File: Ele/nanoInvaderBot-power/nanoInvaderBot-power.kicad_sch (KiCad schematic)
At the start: 10 parts, among them J1 S6B-ZR-SM4A-TF(LF)(SN), J2 S6B-ZR-SM4A-TF(LF)(SN), J3 1746142-1, U3 MP2672AGD-0000-Z

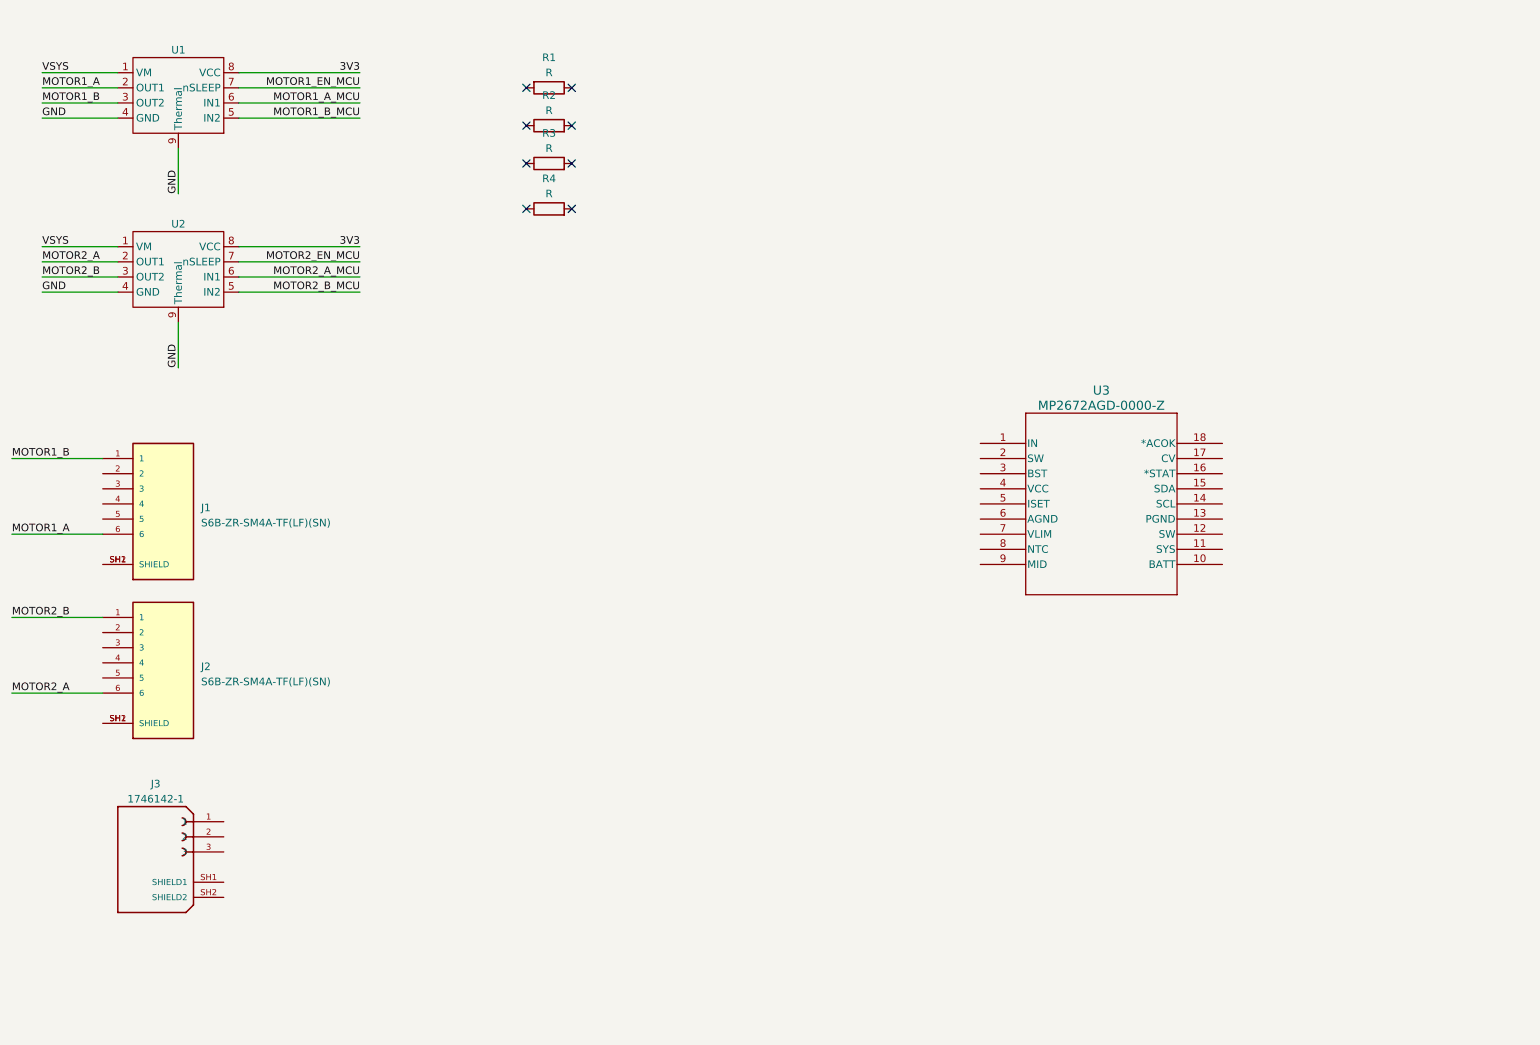
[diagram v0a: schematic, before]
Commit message: Placed components in power board
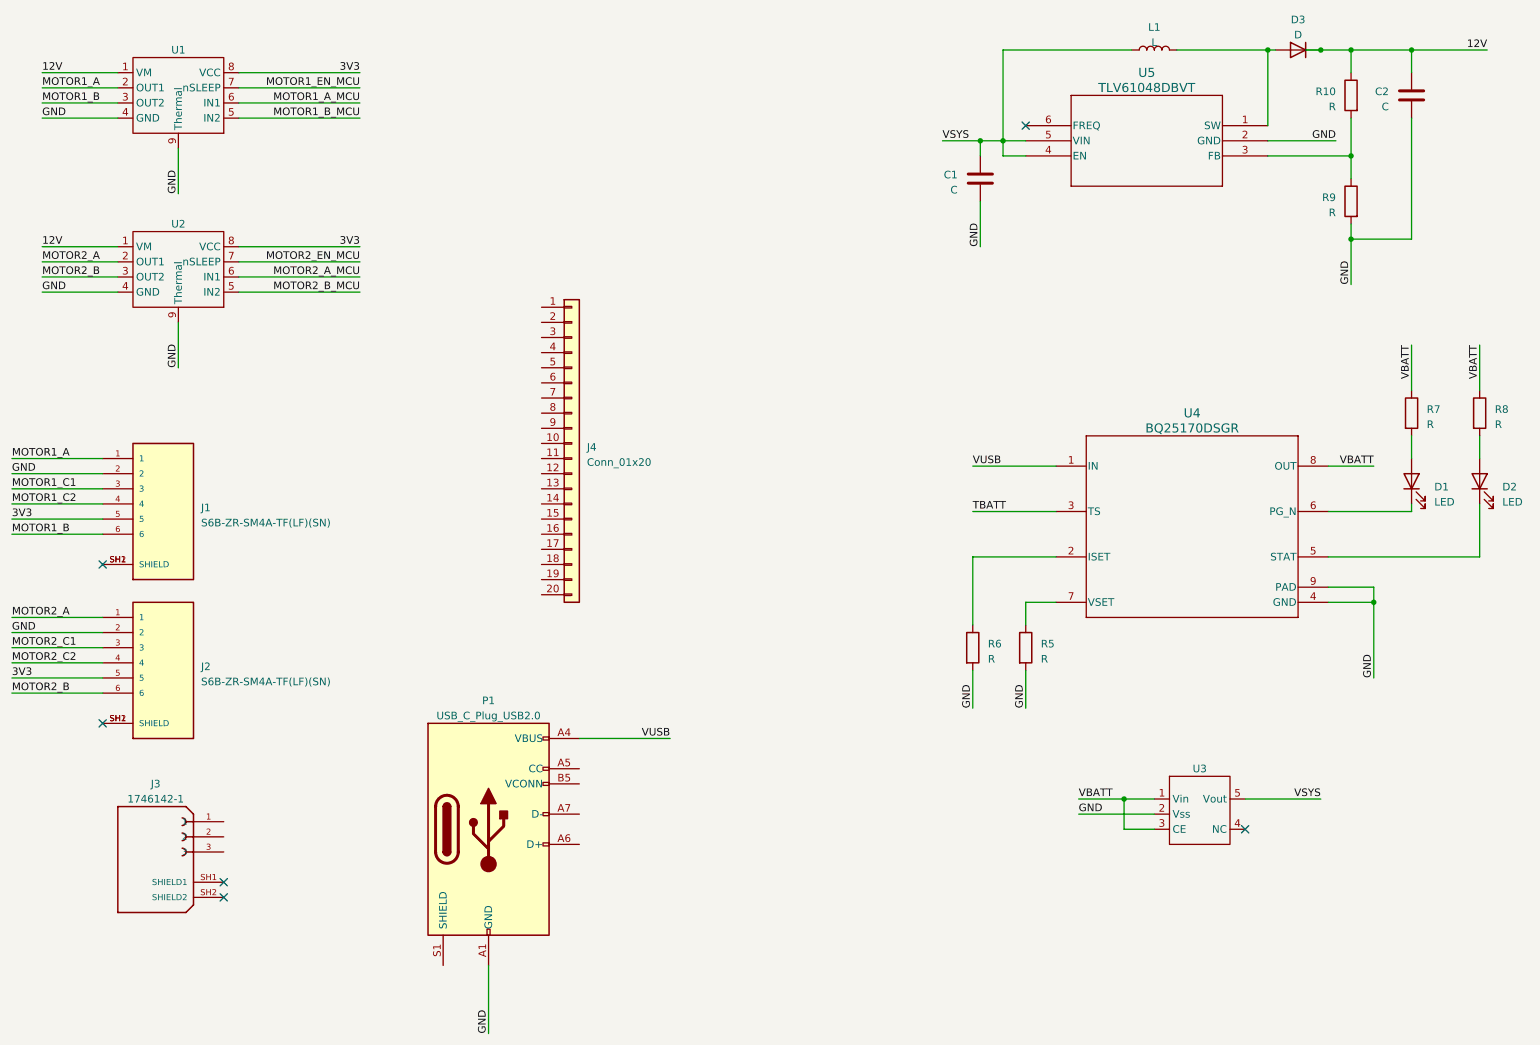
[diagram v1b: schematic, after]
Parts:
- removed R1, R2, R3, R4: R, Resistor_SMD:R_1206_3216Metric, symbol Device:R
- removed U3: MP2672AGD-0000-Z, Components:QFN-18_MP2672A_MNP, symbol MP2672:MP2672AGD-0000-Z
- added C1, C2: C, symbol Device:C
- added D1, D2: LED, LED_SMD:LED_0603_1608Metric, symbol Device:LED
- added D3: D, symbol Device:D
- added J4: Conn_01x20, footprints:TE_2-1734839-0, symbol Connector_Generic:Conn_01x20
- added L1: L, symbol Device:L
- added P1: USB_C_Plug_USB2.0, Connector_USB:USB_C_Receptacle_GCT_USB4135-GF-A_6P_TopMnt_Horizontal, symbol Connector:USB_C_Plug_USB2.0
- added R10, R9: R, symbol Device:R
- added R5, R6, R7, R8: R, Resistor_SMD:R_0603_1608Metric, symbol Device:R
- added U3: ~, Package_TO_SOT_SMD:SOT-23-5, symbol XC8111:XC8111-MR-G
- added U4: BQ25170DSGR, footprints:BQ25170DSGR_NV, symbol BQ25170DSGR:BQ25170DSGR
- added U5: TLV61048DBVT, SOT23-6_DBV_TEX, symbol TLV61048DBVT:TLV61048DBVT
- J1, J2: footprint Components:JST_S6B-ZR-SM4A-TF(LF)(SN) -> footprints:JST_S6B-ZR-SM4A-TF(LF)(SN)
- J3: footprint Components:TE_1746142-1 -> footprints:TE_1746142-1
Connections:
- net 3V3: now also J1.5, J2.5
- net GND: now also J1.2, J2.2, C1.2, C2.2, P1.A1 (GND), P1.A12 (GND), P1.B1 (GND), P1.B12 (GND), R5.2, R6.2, R9.2, U3.2 (Vss), U4.4 (GND), U4.9 (PAD), U5.2 (GND)
- net MOTOR1_A: now also J1.1; no longer J1.6
- net MOTOR1_B: now also J1.6; no longer J1.1
- net MOTOR2_A: now also J2.1; no longer J2.6
- net MOTOR2_B: now also J2.6; no longer J2.1
- net VSYS: now also C1.1, L1.2, U3.5 (Vout), U5.4 (EN), U5.5 (VIN); no longer U1.1 (VM), U2.1 (VM)
- net MOTOR2_C1: now reaches J2.3
- net MOTOR2_C2: now reaches J2.4
- net MOTOR1_C1: now reaches J1.3
- net MOTOR1_C2: now reaches J1.4
- new net: R6.1, U4.2 (ISET)
- new net: D2.1 (K), U4.5 (STAT)
- new net: D1.1 (K), U4.6 (PG_N)
- new net: R5.1, U4.7 (VSET)
- new net: R10.2, R9.1, U5.3 (FB)
- new net: D2.2 (A), R8.2
- new net: D1.2 (A), R7.2
- new net: D3.2 (A), L1.1, U5.1 (SW)
- new net 12V: C2.1, D3.1 (K), R10.1, U1.1 (VM), U2.1 (VM)
- new net TBATT: U4.3 (TS)
- new net VBATT: R7.1, R8.1, U3.1 (Vin), U3.3 (CE), U4.8 (OUT)
- new net VUSB: P1.A4 (VBUS), P1.A9 (VBUS), P1.B4 (VBUS), P1.B9 (VBUS), U4.1 (IN)
- no-connect marks 8 -> 6

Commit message: Intermediate state -power layer almost done
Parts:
- removed P1: USB_C_Plug_USB2.0, Connector_USB:USB_C_Receptacle_GCT_USB4135-GF-A_6P_TopMnt_Horizontal, symbol Connector:USB_C_Plug_USB2.0
- added C10, C4, C6, C7, C8, C9: C, Capacitor_SMD:C_0603_1608Metric, symbol Device:C
- added C3, C5: C, Capacitor_SMD:C_1210_3225Metric, symbol Device:C
- added R1: R, Resistor_SMD:R_0402_1005Metric, symbol Device:R
- added SW1: SW_SPDT, Button_Switch_SMD:SW_SPDT_PCM12, symbol Switch:SW_SPDT
- C1: footprint (none) -> Capacitor_SMD:C_1210_3225Metric; MPN (none) -> GCM32ER71E106KA57L
- C2: footprint (none) -> Capacitor_SMD:C_1210_3225Metric
- D1, D2: footprint LED_SMD:LED_0603_1608Metric -> Resistor_SMD:R_0402_1005Metric
- D3: footprint (none) -> footprints:SDO_B120AF_DIO
- L1: footprint (none) -> footprints:IND_SWPA5040S_SNL
- R10, R9: footprint (none) -> Resistor_SMD:R_0402_1005Metric
- R5, R6, R7, R8: footprint Resistor_SMD:R_0603_1608Metric -> Resistor_SMD:R_0402_1005Metric
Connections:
- net MOTOR1_C1 is gone; now on net MOTOR1_ENC1: J1.3
- net MOTOR1_C2 is gone; now on net MOTOR1_ENC2: J1.4
- net MOTOR2_C1 is gone; now on net MOTOR2_ENC1: J2.3
- net MOTOR2_C2 is gone; now on net MOTOR2_ENC2: J2.4
- net 12V: now also C3.1, C5.1
- net 3V3: now also J4.11 (Pin_11), C4.1, C6.1
- net GND: now also J1.SH1 (SHIELD), J1.SH2 (SHIELD), J2.SH1 (SHIELD), J2.SH2 (SHIELD), J4.17 (Pin_17), J4.18 (Pin_18), J4.3 (Pin_3), J4.4 (Pin_4), C10.2, C3.2, C4.2, C5.2, C6.2, C7.2, C8.2, C9.2, R1.2, SW1.3 (C)
- net MOTOR1_A_MCU: now also J4.6 (Pin_6)
- net MOTOR1_B_MCU: now also J4.5 (Pin_5)
- net MOTOR1_EN_MCU: now also J4.7 (Pin_7)
- net MOTOR2_A_MCU: now also J4.15 (Pin_15)
- net MOTOR2_B_MCU: now also J4.14 (Pin_14)
- net MOTOR2_EN_MCU: now also J4.16 (Pin_16)
- net VBATT: now also C8.1, C9.1, SW1.1 (A); no longer U3.3 (CE)
- net VSYS: now also J4.1 (Pin_1), J4.2 (Pin_2), C10.1
- net VUSB: now also J4.19 (Pin_19), J4.20 (Pin_20), C7.1
- net SYS_EN: now reaches J4.10 (Pin_10)
- net SYS_EN: now also U3.3 (CE), R1.1, SW1.2 (B)
- net MOTOR2_ENC1: now reaches J4.12 (Pin_12)
- net MOTOR2_ENC2: now reaches J4.13 (Pin_13)
- net MOTOR1_ENC1: now reaches J4.8 (Pin_8)
- net MOTOR1_ENC2: now reaches J4.9 (Pin_9)
- no-connect marks 6 -> 4
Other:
- moved on the sheet: D1, D3, J4, R7, U3

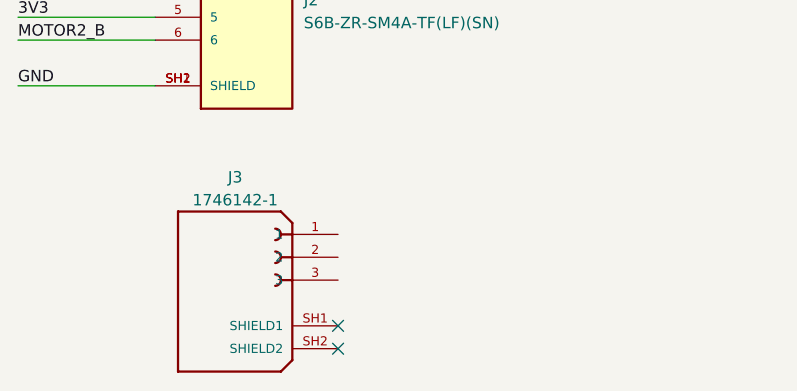
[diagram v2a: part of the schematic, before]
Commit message: Power side done, logic side cleanup
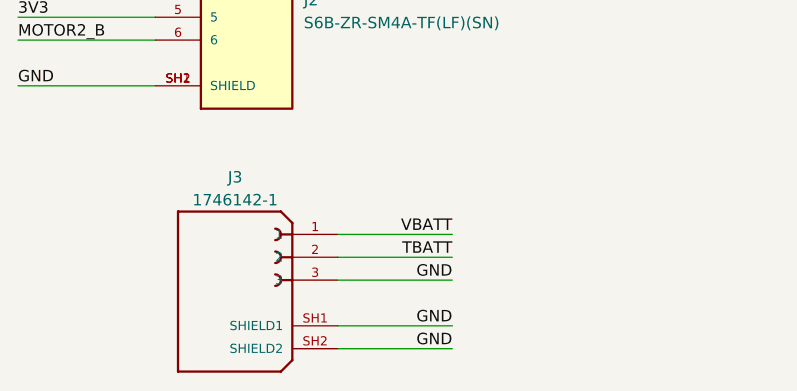
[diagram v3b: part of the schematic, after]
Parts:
- D1, D2: footprint Resistor_SMD:R_0402_1005Metric -> LED_SMD:LED_0402_1005Metric
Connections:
- net GND: now also J3.3, J3.SH1 (SHIELD1), J3.SH2 (SHIELD2)
- net TBATT: now also J3.2
- net VBATT: now also J3.1
- no-connect marks 4 -> 2
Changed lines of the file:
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@@
   (no_connect (at 229.87 146.05))
   (no_connect (at 191.77 35.56))
-  (no_connect (at 57.15 162.56))
-  (no_connect (at 57.15 165.1))
   (wire (pts (xy 191.77 115.57) (xy 196.85 115.57))
     (stroke (width 0) (type default))
@@
     (stroke (width 0) (type default))
   )
+  (wire (pts (xy 57.15 152.4) (xy 69.85 152.4))
+    (stroke (width 0) (type default))
+  )
   (wire (pts (xy 246.38 151.13) (xy 246.38 157.48))
     (stroke (width 0) (type default))
@@
     (stroke (width 0) (type default))
   )
+  (wire (pts (xy 57.15 162.56) (xy 69.85 162.56))
+    (stroke (width 0) (type default))
+  )
   (wire (pts (xy 246.38 54.61) (xy 246.38 62.23))
     (stroke (width 0) (type default))
@@
     (stroke (width 0) (type default))
   )
+  (wire (pts (xy 57.15 165.1) (xy 69.85 165.1))
+    (stroke (width 0) (type default))
+  )
   (wire (pts (xy 59.69 26.67) (xy 80.01 26.67))
     (stroke (width 0) (type default))
@@
     (stroke (width 0) (type default))
   )
+  (wire (pts (xy 57.15 157.48) (xy 69.85 157.48))
+    (stroke (width 0) (type default))
+  )
   (wire (pts (xy 246.38 40.64) (xy 246.38 34.29))
     (stroke (width 0) (type default))
@@
     (stroke (width 0) (type default))
   )
+  (wire (pts (xy 57.15 154.94) (xy 69.85 154.94))
+    (stroke (width 0) (type default))
+  )
   (wire (pts (xy 59.69 34.29) (xy 80.01 34.29))
     (stroke (width 0) (type default))
@@
     (effects (font (size 1.27 1.27)) (justify left bottom))
   )
+  (label "TBATT" (at 69.85 154.94 180) (fields_autoplaced)
+    (effects (font (size 1.27 1.27)) (justify right bottom))
+  )
   (label "GND" (at 93.98 41.91 90) (fields_autoplaced)
     (effects (font (size 1.27 1.27)) (justify left bottom))
@@
     (effects (font (size 1.27 1.27)) (justify left bottom))
   )
+  (label "GND" (at 69.85 165.1 180) (fields_autoplaced)
+    (effects (font (size 1.27 1.27)) (justify right bottom))
+  )
+  (label "VBATT" (at 69.85 152.4 180) (fields_autoplaced)
+    (effects (font (size 1.27 1.27)) (justify right bottom))
+  )
   (label "MOTOR1_B_MCU" (at 80.01 34.29 180) (fields_autoplaced)
     (effects (font (size 1.27 1.27)) (justify right bottom))
@@
     (effects (font (size 1.27 1.27)) (justify left bottom))
   )
+  (label "GND" (at 69.85 162.56 180) (fields_autoplaced)
+    (effects (font (size 1.27 1.27)) (justify right bottom))
+  )
   (label "GND" (at 243.84 38.1 180) (fields_autoplaced)
+    (effects (font (size 1.27 1.27)) (justify right bottom))
+  )
+  (label "GND" (at 69.85 157.48 180) (fields_autoplaced)
     (effects (font (size 1.27 1.27)) (justify right bottom))
   )
@@
       (effects (font (size 1.27 1.27)) (justify right))
     )
-    (property "Footprint" "Resistor_SMD:R_0402_1005Metric" (at 267.97 95.25 0)
+    (property "Footprint" "LED_SMD:LED_0402_1005Metric" (at 267.97 95.25 0)
       (effects (font (size 1.27 1.27)) hide)
     )
@@
       (effects (font (size 1.27 1.27)) (justify right))
     )
-    (property "Footprint" "Resistor_SMD:R_0402_1005Metric" (at 260.35 95.25 0)
-      (effects (font (size 1.27 1.27)) hide)
-    )
+    (property "Footprint" "LED_SMD:LED_0402_1005Metric" (at 260.35 95.25 0)
+      (effects (font (size 1.27 1.27)) hide)
+    )

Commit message: Intermediate state after v23.10
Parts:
- C1, C2: value C -> 1uF
- R1: value R -> 10k
- R10: value R -> 1M5
- R5: value R -> 36k
- R6: value R -> 620
- R9: value R -> 110k
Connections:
- net 3V3: now also J4.10 (Pin_10)
- net SYS_EN: no longer J4.10 (Pin_10)
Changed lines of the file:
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@@
     (effects (font (size 1.27 1.27)) (justify left bottom))
   )
-  (label "SYS_EN" (at 128.27 74.93 0) (fields_autoplaced)
+  (label "3V3" (at 128.27 74.93 0) (fields_autoplaced)
     (effects (font (size 1.27 1.27)) (justify left bottom))
   )
@@
       (effects (font (size 1.27 1.27)) (justify left))
     )
-    (property "Value" "R" (at 243.84 50.165 0)
+    (property "Value" "110k" (at 243.84 50.165 0)
       (effects (font (size 1.27 1.27)) (justify left))
     )
@@
       (effects (font (size 1.27 1.27)) (justify left))
     )
-    (property "Value" "R" (at 208.28 154.305 0)
+    (property "Value" "10k" (at 208.28 154.305 0)
       (effects (font (size 1.27 1.27)) (justify left))
     )
@@
       (effects (font (size 1.27 1.27)) (justify left))
     )
-    (property "Value" "C" (at 180.34 46.355 0)
+    (property "Value" "1uF" (at 180.34 46.355 0)
       (effects (font (size 1.27 1.27)) (justify left))
     )
@@
       (effects (font (size 1.27 1.27)) (justify left))
     )
-    (property "Value" "R" (at 185.42 125.095 0)
+    (property "Value" "620" (at 185.42 125.095 0)
       (effects (font (size 1.27 1.27)) (justify left))
     )
@@
       (effects (font (size 1.27 1.27)) (justify left))
     )
-    (property "Value" "C" (at 252.73 32.385 0)
+    (property "Value" "1uF" (at 252.73 32.385 0)
       (effects (font (size 1.27 1.27)) (justify left))
     )
@@
       (effects (font (size 1.27 1.27)) (justify left))
     )
-    (property "Value" "R" (at 194.31 125.095 0)
+    (property "Value" "36k" (at 194.31 125.095 0)
       (effects (font (size 1.27 1.27)) (justify left))
     )
@@
       (effects (font (size 1.27 1.27)) (justify left))
     )
-    (property "Value" "R" (at 243.84 32.385 0)
-      (effects (font (size 1.27 1.27)) (justify left))
-    )
+    (property "Value" "1M5" (at 243.84 32.385 0)
+      (effects (font (size 1.27 1.27)) (justify left))
+    )

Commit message: Modifications for first running proto
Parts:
- R10: value 1M5 -> 1M
- R7, R8: value R -> 1k
- R9: value 110k -> 100k
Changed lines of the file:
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@@
     )
   )
-  (symbol (lib_id "Device:R") (at 246.38 48.26 0) (mirror y) (unit 1)
-    (in_bom yes) (on_board yes) (dnp no) (fields_autoplaced)
+  (symbol (lib_id "Device:R") (at 246.38 48.26 0) (unit 1)
+    (in_bom yes) (on_board yes) (dnp no)
     (property "Reference" "R9" (at 243.84 47.625 0)
-      (effects (font (size 1.27 1.27)) (justify left))
-    )
-    (property "Value" "110k" (at 243.84 50.165 0)
-      (effects (font (size 1.27 1.27)) (justify left))
-    )
-    (property "Footprint" "Resistor_SMD:R_0402_1005Metric" (at 248.158 48.26 90)
+      (effects (font (size 1.27 1.27)) (justify right))
+    )
+    (property "Value" "100k" (at 243.84 50.165 0)
+      (effects (font (size 1.27 1.27)) (justify right))
+    )
+    (property "Footprint" "Resistor_SMD:R_0402_1005Metric" (at 244.602 48.26 90)
       (effects (font (size 1.27 1.27)) hide)
     )
@@
       (effects (font (size 1.27 1.27)) (justify left))
     )
-    (property "Value" "R" (at 262.89 85.725 0)
+    (property "Value" "1k" (at 262.89 85.725 0)
       (effects (font (size 1.27 1.27)) (justify left))
     )
@@
       (effects (font (size 1.27 1.27)) (justify left))
     )
-    (property "Value" "R" (at 270.51 85.725 0)
+    (property "Value" "1k" (at 270.51 85.725 0)
       (effects (font (size 1.27 1.27)) (justify left))
     )
@@
     )
   )
-  (symbol (lib_id "Device:R") (at 246.38 30.48 0) (mirror y) (unit 1)
-    (in_bom yes) (on_board yes) (dnp no) (fields_autoplaced)
+  (symbol (lib_id "Device:R") (at 246.38 30.48 0) (unit 1)
+    (in_bom yes) (on_board yes) (dnp no)
     (property "Reference" "R10" (at 243.84 29.845 0)
-      (effects (font (size 1.27 1.27)) (justify left))
-    )
-    (property "Value" "1M5" (at 243.84 32.385 0)
-      (effects (font (size 1.27 1.27)) (justify left))
-    )
-    (property "Footprint" "Resistor_SMD:R_0402_1005Metric" (at 248.158 30.48 90)
-      (effects (font (size 1.27 1.27)) hide)
-    )
+      (effects (font (size 1.27 1.27)) (justify right))
+    )
+    (property "Value" "1M" (at 243.84 32.385 0)
+      (effects (font (size 1.27 1.27)) (justify right))
+    )
+    (property "Footprint" "Resistor_SMD:R_0402_1005Metric" (at 244.602 30.48 90)
+      (effects (font (size 1.27 1.27)) hide)
+    )
